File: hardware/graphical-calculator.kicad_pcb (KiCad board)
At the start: 2 copper layers, 90 x 155 mm, 43 parts, among them SW0 SW_Omron_B3FS, SW1 SW_Omron_B3FS, SW2 SW_Omron_B3FS, SW3 SW_Omron_B3FS, SW4 SW_Omron_B3FS, SW5 SW_Omron_B3FS, SW6 SW_Omron_B3FS, SW7 SW_Omron_B3FS, SW8 SW_Omron_B3FS, SW9 SW_Omron_B3FS, U1 RASPBERRY_PI_ZERO_2_W, U4 MCP23017_SO, U5 MCP23017_SO

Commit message: update pcb and 3d model
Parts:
- removed SWZOOM1: SW_Push_SPDT, Button_Switch_SMD:SW_SPDT_CK_JS102011SAQN
- added SWIN1: SW_Omron_B3FS, Button_Switch_SMD:SW_SPST_Omron_B3FS-105xP, F.Cu at (78.0, 103.8)
- added SWOUT1: SW_Omron_B3FS, Button_Switch_SMD:SW_SPST_Omron_B3FS-105xP, F.Cu at (78.0, 111.2)
- SWRAD1: footprint Button_Switch_SMD:SW_SPDT_CK_JS102011SAQN -> JS102011JCQN:SW_JS102011JCQN
- moved SWSHIFT1 3.50 mm to (78.0, 95.0)
- moved SWRAD1 1.58 mm to (148.2, 108.5)
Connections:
- SWRAD1 pad 1: RAD -> DEG
- SWRAD1 pad 2: DEG -> GND
- SWRAD1 pad 3: GND -> RAD
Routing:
- net GND: track 727.0 -> 752.9 mm
- net OUT: track 70.7 -> 78.6 mm
- net DEG: track 91.2 -> 97.5 mm
- net IN: track 87.5 -> 83.9 mm
- net SHIFT: track 64.8 -> 61.3 mm

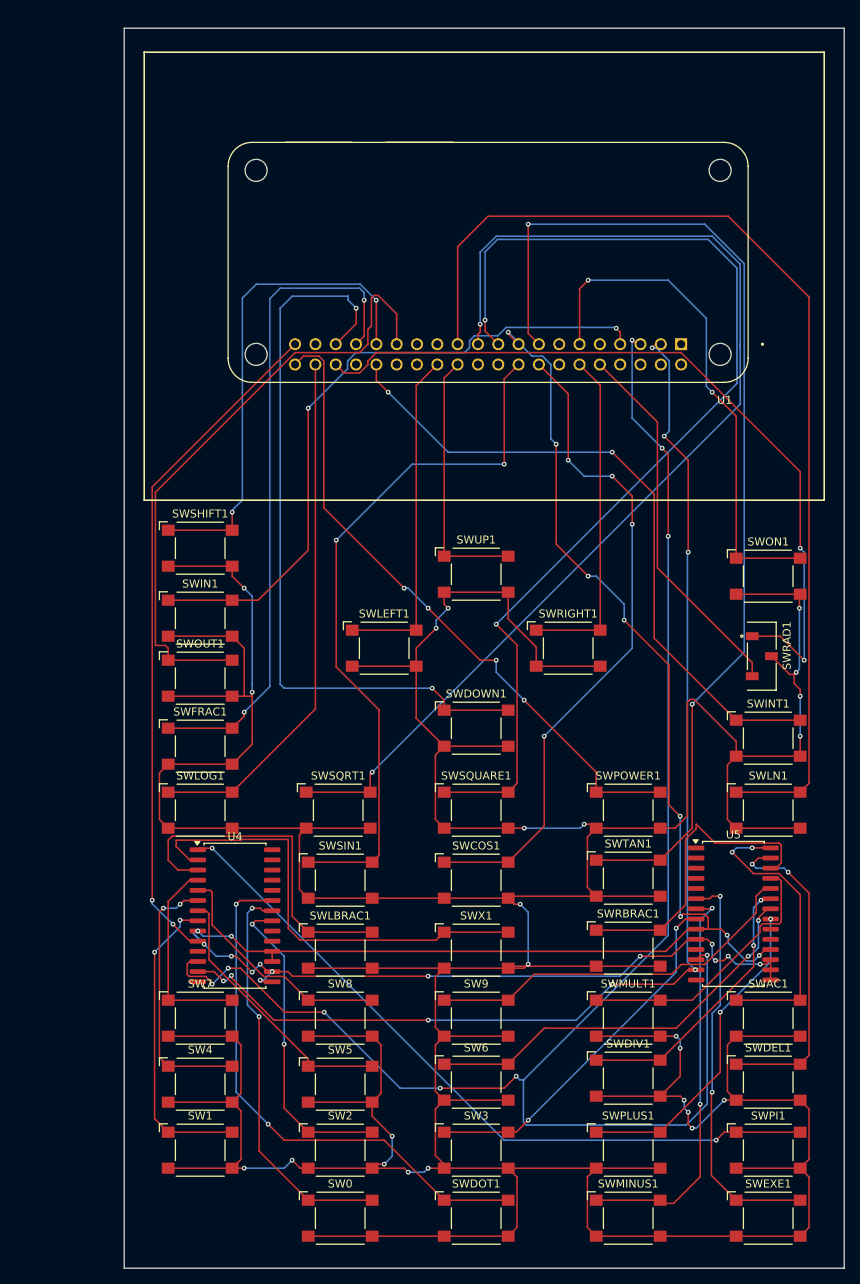
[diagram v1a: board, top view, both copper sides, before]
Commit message: redo board with matrix, tht, cad with screen
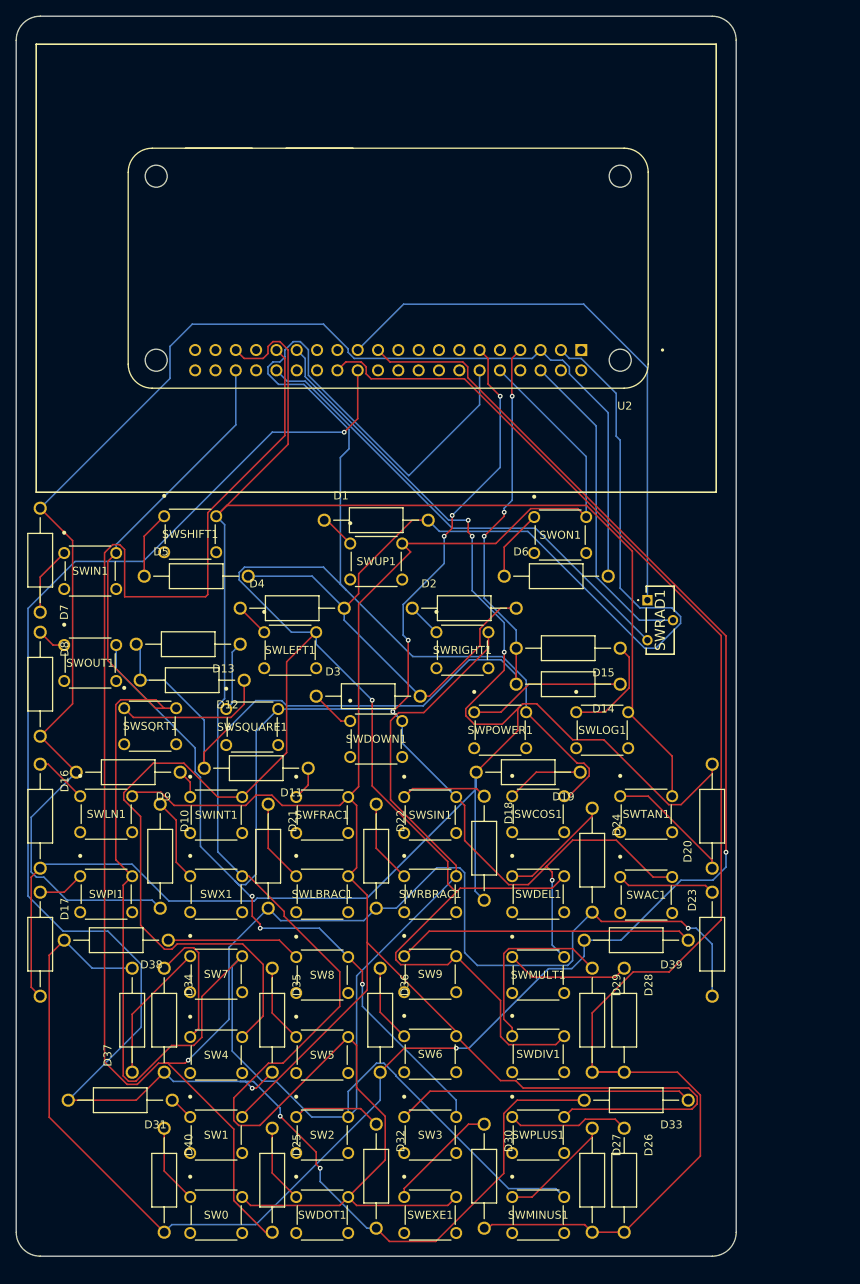
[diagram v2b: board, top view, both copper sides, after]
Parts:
- removed U1: RASPBERRY_PI_ZERO_2_W, RPI_Zero2W:MODULE_RASPBERRY_PI_ZERO_2_W
- removed U4, U5: MCP23017_SO, Package_SO:SOIC-28W_7.5x17.9mm_P1.27mm
- added D1: D, 1N4148 _DO-35_:DIOAD1300W80L670D310, F.Cu at (100.0, 91.5)
- added D10: D, 1N4148 _DO-35_:DIOAD1300W80L670D310, F.Cu at (73.0, 133.5)
- added D11: D, 1N4148 _DO-35_:DIOAD1300W80L670D310, F.Cu at (85.0, 122.5)
- added D12: D, 1N4148 _DO-35_:DIOAD1300W80L670D310, F.Cu at (77.0, 111.5)
- added D13: D, 1N4148 _DO-35_:DIOAD1300W80L670D310, F.Cu at (76.5, 107.0)
- added D14: D, 1N4148 _DO-35_:DIOAD1300W80L670D310, F.Cu at (124.0, 112.0)
- added D15: D, 1N4148 _DO-35_:DIOAD1300W80L670D310, F.Cu at (124.0, 107.5)
- added D16: D, 1N4148 _DO-35_:DIOAD1300W80L670D310, F.Cu at (58.0, 128.5)
- added D17: D, 1N4148 _DO-35_:DIOAD1300W80L670D310, F.Cu at (58.0, 144.5)
- added D18: D, 1N4148 _DO-35_:DIOAD1300W80L670D310, F.Cu at (113.5, 132.5)
- added D19: D, 1N4148 _DO-35_:DIOAD1300W80L670D310, F.Cu at (119.0, 123.0)
- added D2: D, 1N4148 _DO-35_:DIOAD1300W80L670D310, F.Cu at (111.0, 102.5)
- added D20: D, 1N4148 _DO-35_:DIOAD1300W80L670D310, F.Cu at (142.0, 128.5)
- added D21: D, 1N4148 _DO-35_:DIOAD1300W80L670D310, F.Cu at (86.5, 133.5)
- added D22: D, 1N4148 _DO-35_:DIOAD1300W80L670D310, F.Cu at (100.0, 133.5)
- added D23: D, 1N4148 _DO-35_:DIOAD1300W80L670D310, F.Cu at (142.0, 144.5)
- added D24: D, 1N4148 _DO-35_:DIOAD1300W80L670D310, F.Cu at (127.0, 134.0)
- added D25: D, 1N4148 _DO-35_:DIOAD1300W80L670D310, F.Cu at (87.0, 174.0)
- added D26: D, 1N4148 _DO-35_:DIOAD1300W80L670D310, F.Cu at (131.0, 174.0)
- added D27: D, 1N4148 _DO-35_:DIOAD1300W80L670D310, F.Cu at (127.0, 174.0)
- added D28: D, 1N4148 _DO-35_:DIOAD1300W80L670D310, F.Cu at (131.0, 154.0)
- added D29: D, 1N4148 _DO-35_:DIOAD1300W80L670D310, F.Cu at (127.0, 154.0)
- added D3: D, 1N4148 _DO-35_:DIOAD1300W80L670D310, F.Cu at (99.0, 113.5)
- added D30: D, 1N4148 _DO-35_:DIOAD1300W80L670D310, F.Cu at (113.5, 173.5)
- added D31: D, 1N4148 _DO-35_:DIOAD1300W80L670D310, F.Cu at (68.0, 164.0)
- added D32: D, 1N4148 _DO-35_:DIOAD1300W80L670D310, F.Cu at (100.0, 173.5)
- added D33: D, 1N4148 _DO-35_:DIOAD1300W80L670D310, F.Cu at (132.5, 164.0)
- added D34: D, 1N4148 _DO-35_:DIOAD1300W80L670D310, F.Cu at (73.5, 154.0)
- added D35: D, 1N4148 _DO-35_:DIOAD1300W80L670D310, F.Cu at (87.0, 154.0)
- added D36: D, 1N4148 _DO-35_:DIOAD1300W80L670D310, F.Cu at (100.5, 154.0)
- added D37: D, 1N4148 _DO-35_:DIOAD1300W80L670D310, F.Cu at (69.5, 154.0)
- added D38: D, 1N4148 _DO-35_:DIOAD1300W80L670D310, F.Cu at (67.5, 144.0)
- added D39: D, 1N4148 _DO-35_:DIOAD1300W80L670D310, F.Cu at (132.5, 144.0)
- added D4: D, 1N4148 _DO-35_:DIOAD1300W80L670D310, F.Cu at (89.5, 102.5)
- added D40: D, 1N4148 _DO-35_:DIOAD1300W80L670D310, F.Cu at (73.5, 174.0)
- added D5: D, 1N4148 _DO-35_:DIOAD1300W80L670D310, F.Cu at (77.5, 98.5)
- added D6: D, 1N4148 _DO-35_:DIOAD1300W80L670D310, F.Cu at (122.5, 98.5)
- added D7: D, 1N4148 _DO-35_:DIOAD1300W80L670D310, F.Cu at (58.0, 96.5)
- added D8: D, 1N4148 _DO-35_:DIOAD1300W80L670D310, F.Cu at (58.0, 112.0)
- added D9: D, 1N4148 _DO-35_:DIOAD1300W80L670D310, F.Cu at (69.0, 123.0)
- added U2: RASPBERRY_PI_ZERO_2_W, RPI-Zero-2W:MODULE_RASPBERRY_PI_ZERO_2_W, F.Cu at (101.5, 60.0)
- SW0, SW1, SW2, SW3, SW4, SW5, SW6, SW7, SW8, SW9, SWAC1, SWCOS1, SWDEL1, SWDIV1, SWDOT1, SWDOWN1, SWEXE1, SWFRAC1, SWIN1, SWINT1, SWLBRAC1, SWLEFT1, SWLN1, SWLOG1, SWMINUS1, SWMULT1, SWON1, SWOUT1, SWPI1, SWPLUS1, SWPOWER1, SWRBRAC1, SWRIGHT1, SWSHIFT1, SWSIN1, SWSQRT1, SWSQUARE1, SWTAN1, SWUP1, SWX1: value SW_Omron_B3FS -> B3F-1050; footprint Button_Switch_SMD:SW_SPST_Omron_B3FS-105xP -> B3F-1050:SW_B3F-1050_OMR
- SWRAD1: value SW_SPDT -> JS102011CQN; footprint JS102011JCQN:SW_JS102011JCQN -> JS102011CQN:JS102011CQN
- moved SWPI1 92.6 mm to (63.0, 136.0)
- moved SWLN1 86.0 mm to (63.0, 126.0)
- moved SWINT1 72.6 mm to (76.7, 126.1)
- moved SWLOG1 48.6 mm to (125.0, 115.5)
- moved SWEXE1 45.6 mm to (103.5, 176.1)
- moved SWDEL1 41.1 mm to (117.0, 136.0)
- moved SWX1 36.9 mm to (76.7, 136.0)
- moved SWSQUARE1 33.7 mm to (81.2, 115.1)
- moved SWON1 30.2 mm to (119.7, 91.1)
- moved SWSQRT1 29.6 mm to (68.5, 115.0)
- moved SWRBRAC1 29.4 mm to (103.5, 136.0)
- moved SWAC1 25.6 mm to (130.5, 136.1)
- moved SWPOWER1 22.8 mm to (112.2, 115.5)
- moved SWDOT1 22.7 mm to (90.0, 176.1)
- moved SW0 18.9 mm to (76.7, 176.1)
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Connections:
- SW0 pad 1: 0 -> Net-(D40-K)
- SW0 pad 2: GND -> COL5
- SW1 pad 1: 1 -> Net-(D31-K)
- SW1 pad 2: GND -> COL1
- SW2 pad 1: 2 -> Net-(D32-K)
- SW2 pad 2: GND -> COL2
- SW3 pad 1: 3 -> Net-(D33-K)
- SW3 pad 2: GND -> COL3
- SW4 pad 1: 4 -> Net-(D34-K)
- SW4 pad 2: GND -> COL4
- SW5 pad 1: 5 -> Net-(D35-K)
- SW5 pad 2: GND -> COL5
- SW6 pad 1: 6 -> Net-(D36-K)
- SW6 pad 2: GND -> COL1
- SW7 pad 1: 7 -> Net-(D37-K)
- SW7 pad 2: GND -> COL2
- SW8 pad 1: 8 -> Net-(D38-K)
- SW8 pad 2: GND -> COL3
- SW9 pad 1: 9 -> Net-(D39-K)
- SW9 pad 2: GND -> COL4
- SWAC1 pad 1: AC -> Net-(D23-K)
- SWAC1 pad 2: GND -> COL3
- SWCOS1 pad 1: COS -> Net-(D19-K)
- SWCOS1 pad 2: GND -> COL4
- SWDEL1 pad 1: DEL -> Net-(D24-K)
- SWDEL1 pad 2: GND -> COL4
- SWDIV1 pad 1: DIV -> Net-(D29-K)
- SWDIV1 pad 2: GND -> COL4
- SWDOT1 pad 1: DOT -> Net-(D25-K)
- SWDOT1 pad 2: GND -> COL5
- SWDOWN1 pad 1: DOWN -> Net-(D3-K)
- SWDOWN1 pad 2: GND -> COL3
- SWEXE1 pad 1: EXE -> Net-(D30-K)
- SWEXE1 pad 2: GND -> COL5
- SWFRAC1 pad 1: FRAC -> Net-(D11-K)
- SWFRAC1 pad 2: GND -> COL1
- SWIN1 pad 1: IN -> Net-(D7-K)
- SWIN1 pad 2: GND -> COL2
- SWINT1 pad 1: INT -> Net-(D9-K)
- SWINT1 pad 2: GND -> COL4
- SWLBRAC1 pad 1: LBRAC -> Net-(D21-K)
- SWLBRAC1 pad 2: GND -> COL1
- SWLEFT1 pad 1: LEFT -> Net-(D4-K)
- SWLEFT1 pad 2: GND -> COL4
- SWLN1 pad 1: LN -> Net-(D16-K)
- SWLN1 pad 2: GND -> COL1
- SWLOG1 pad 1: LOG -> Net-(D15-K)
- SWLOG1 pad 2: GND -> COL5
- SWMINUS1 pad 1: MINUS -> Net-(D27-K)
- SWMINUS1 pad 2: GND -> COL2
- SWMULT1 pad 1: MULT -> Net-(D28-K)
- SWMULT1 pad 2: GND -> COL3
- SWON1 pad 1: ON -> Net-(D6-K)
- SWON1 pad 2: GND -> COL1
- SWOUT1 pad 1: OUT -> Net-(D8-K)
- SWOUT1 pad 2: GND -> COL3
- SWPI1 pad 1: PI -> Net-(D17-K)
- SWPI1 pad 2: GND -> COL2
- SWPLUS1 pad 1: PLUS -> Net-(D26-K)
- SWPLUS1 pad 2: GND -> COL1
- SWPOWER1 pad 1: POWER -> Net-(D14-K)
- SWPOWER1 pad 2: GND -> COL4
- SWRBRAC1 pad 1: RBRAC -> Net-(D22-K)
- SWRBRAC1 pad 2: GND -> COL2
- SWRIGHT1 pad 1: RIGHT -> Net-(D2-K)
- SWRIGHT1 pad 2: GND -> COL2
- SWSHIFT1 pad 1: SHIFT -> Net-(D5-K)
- SWSHIFT1 pad 2: GND -> COL5
- SWSIN1 pad 1: SIN -> Net-(D18-K)
- SWSIN1 pad 2: GND -> COL3
- SWSQRT1 pad 1: SQRT -> Net-(D12-K)
- SWSQRT1 pad 2: GND -> COL2
- SWSQUARE1 pad 1: SQUARE -> Net-(D13-K)
- SWSQUARE1 pad 2: GND -> COL3
- SWTAN1 pad 1: TAN -> Net-(D20-K)
- SWTAN1 pad 2: GND -> COL5
- SWUP1 pad 1: UP -> Net-(D1-K)
- SWUP1 pad 2: GND -> COL1
- SWX1 pad 1: X -> Net-(D10-K)
- SWX1 pad 2: GND -> COL5
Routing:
- net GND: track 752.9 -> 40.5 mm, vias 24 -> 0
- net COL4: track 0.00 -> 338.0 mm, vias 0 -> 1
- net COL5: track 0.00 -> 282.5 mm
- net COL2: track 0.00 -> 278.4 mm
- net ROW5: track 0.00 -> 264.5 mm, vias 0 -> 2
- net COL3: track 0.00 -> 239.2 mm, vias 0 -> 9
- net ROW8: track 0.00 -> 233.5 mm, vias 0 -> 2
- net COL1: track 0.00 -> 228.9 mm
- net ROW7: track 0.00 -> 225.5 mm, vias 0 -> 4
- net ROW4: track 0.00 -> 209.1 mm, vias 0 -> 3
- net SCL: track 206.1 -> 0.00 mm, vias 9 -> 0
- net ROW6: track 0.00 -> 184.9 mm
- net ROW2: track 0.00 -> 180.6 mm
- net Net-(U1-GND_39): track 174.1 -> 0.00 mm, vias 14 -> 0
- net Net-(U1-3V3_17): track 169.8 -> 0.00 mm, vias 10 -> 0
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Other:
- outline, holes or cut-outs redrawn
